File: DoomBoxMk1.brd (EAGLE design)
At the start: 41.9 x 47 mm, 14 parts, among them Q1 BC109, SW1 DPDT

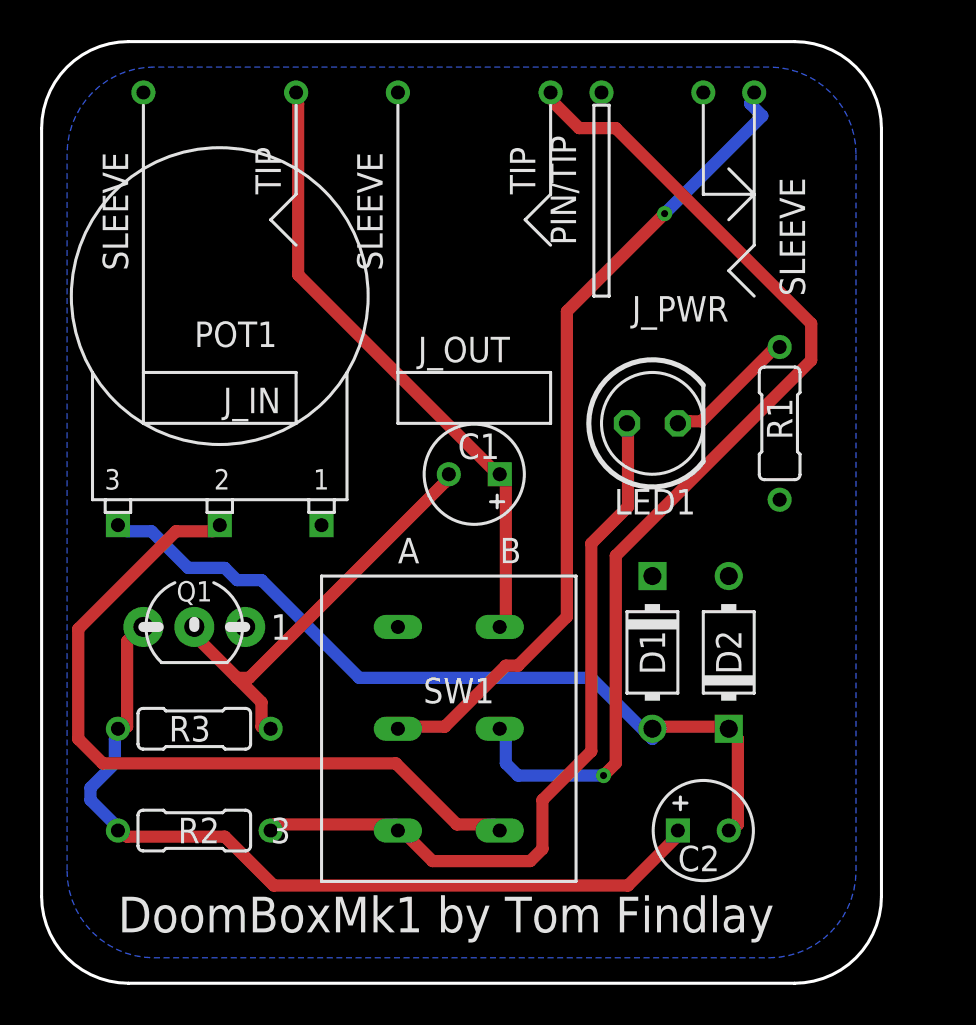
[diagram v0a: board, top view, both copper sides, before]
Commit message: Added XR logo and filtered power version
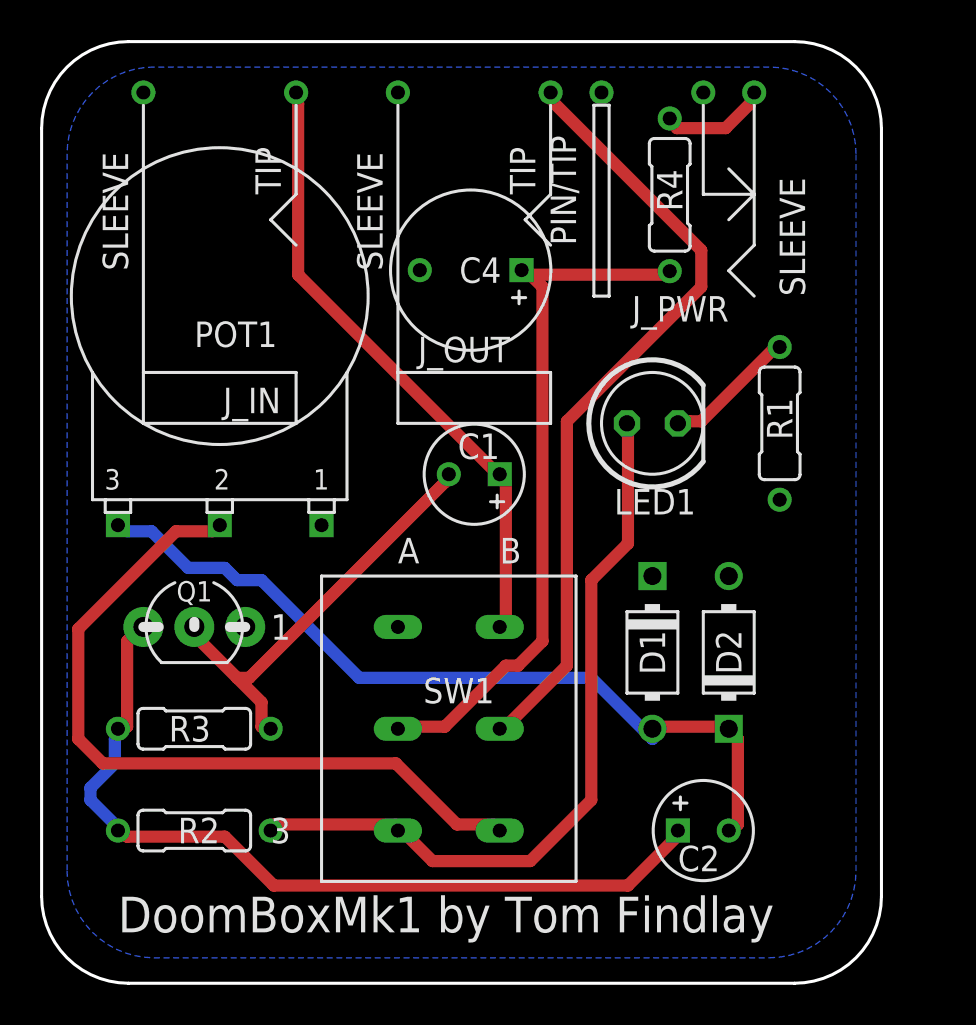
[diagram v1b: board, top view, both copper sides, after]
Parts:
- added C4: (no value), gm-caps-electro-pol:080_035_2
- added R4: 50, gm-resistors:R0207/3
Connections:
- new net +9V_UNF: J_PWR.SLEEVE, R4.1
- net +9V: now also C4.+, R4.2; no longer J_PWR.SLEEVE
- net GND: now also C4.-
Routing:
- net OUT_J: track 51.7 -> 39.1 mm, vias 1 -> 0
- net +9V: track 41.2 -> 35.0 mm, vias 1 -> 0
- net +9V_UNF: track 0.00 -> 5.36 mm
